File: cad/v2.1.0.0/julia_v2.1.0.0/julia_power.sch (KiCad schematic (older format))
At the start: 50 parts, among them J1 Barrel_Jack_Switch, U2 AZ1117-3.3, U3 AZ1117-2.5, U4 NCP565ST12T3G

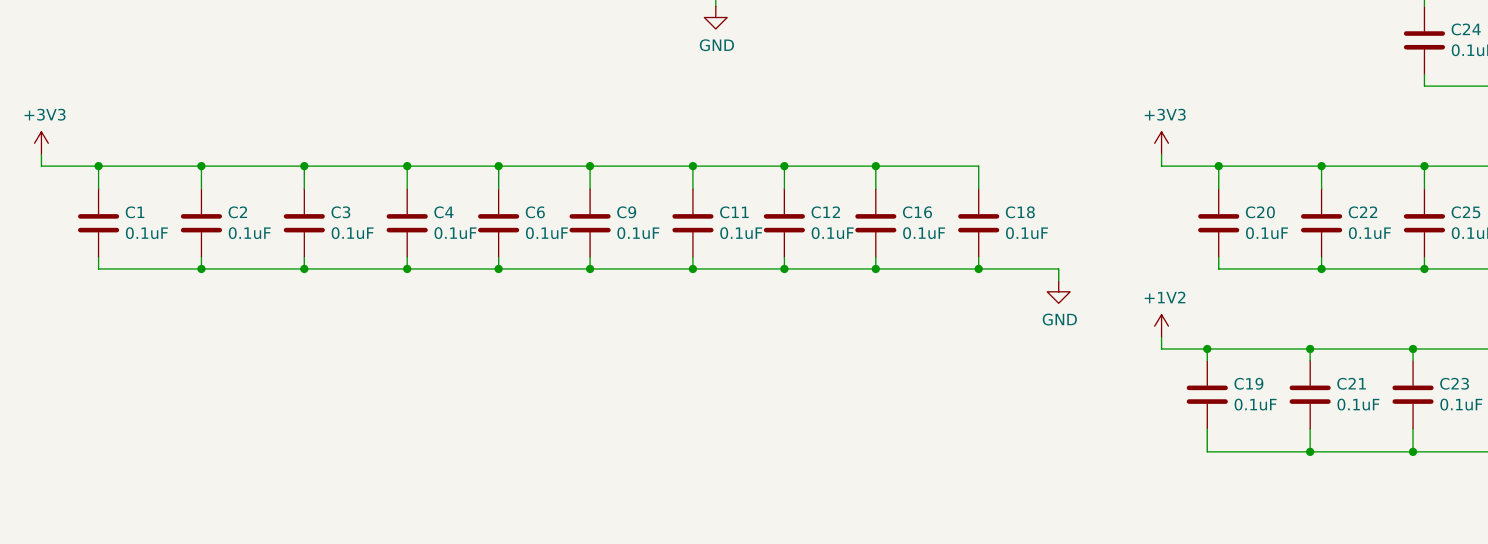
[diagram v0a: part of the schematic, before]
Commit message: v2.1.0.0: changed connector, ERC, annotation/footprint assignment
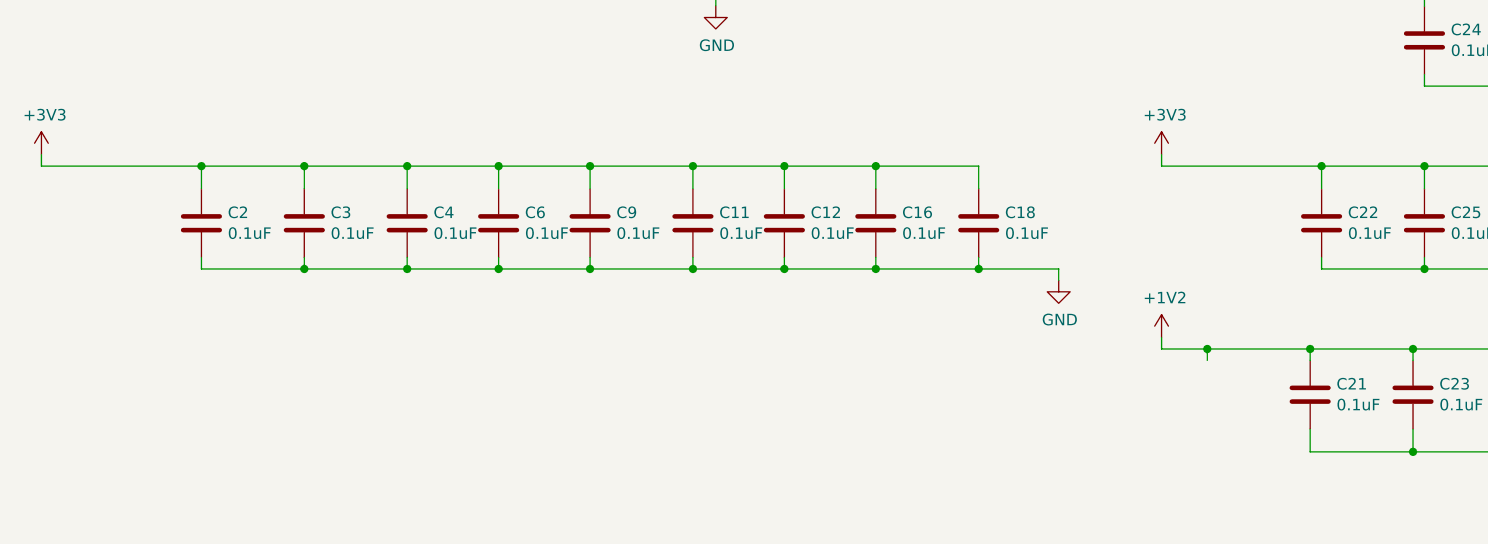
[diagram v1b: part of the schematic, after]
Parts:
- removed C1, C19, C20: 0.1uF, symbol Device:C
- C10, C11, C12, C13, C16, C18, C2, C21, C22, C23, C24, C25, C26, C27, C28, C29, C3, C30, C31, C32, C33, C34, C35, C36, C37, C38, C39, C4, C40, C6, C9: footprint (none) -> Capacitor_SMD:C_0402_1005Metric
- C14, C15, C7, C8: footprint (none) -> Capacitor_SMD:C_0603_1608Metric
- C17, C5: footprint (none) -> Capacitor_Tantalum_SMD:CP_EIA-2012-15_AVX-P
- F1: footprint (none) -> Fuse:Fuse_1206_3216Metric
- J1: footprint (none) -> ik:BarrelJack_GCT_DCJ200-05-A-K1-A_SMD_Horizontal
- TP1, TP2, TP3, TP4, TP5: footprint (none) -> TestPoint:TestPoint_THTPad_D1.0mm_Drill0.5mm
- U2, U3, U4: footprint (none) -> Package_TO_SOT_SMD:SOT-223-3_TabPin2

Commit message: Layout complete(?)
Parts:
- removed C21, C23, C26, C30, C34, C36, C40: 0.1uF, Capacitor_SMD:C_0402_1005Metric, symbol Device:C
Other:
- moved on the sheet: C32, C38
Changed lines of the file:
@@
 $EndComp
 Wire Wire Line
-	9850 6000 9400 6000
-Connection ~ 9850 6000
-Wire Wire Line
-	9850 5900 9850 6000
-Wire Wire Line
-	9400 6000 8950 6000
-Connection ~ 9400 6000
-Wire Wire Line
-	9400 5900 9400 6000
-Wire Wire Line
-	8950 6000 8500 6000
-Connection ~ 8950 6000
-Wire Wire Line
-	8950 5900 8950 6000
-Wire Wire Line
-	8500 6000 8050 6000
-Connection ~ 8500 6000
-Wire Wire Line
-	8500 5900 8500 6000
-Wire Wire Line
-	8050 6000 7600 6000
-Connection ~ 8050 6000
-Wire Wire Line
-	8050 5900 8050 6000
-Wire Wire Line
-	7600 6000 7150 6000
-Connection ~ 7600 6000
-Wire Wire Line
-	7600 5900 7600 6000
-Wire Wire Line
-	7150 6000 6700 6000
-Connection ~ 7150 6000
-Wire Wire Line
-	7150 5900 7150 6000
-Wire Wire Line
-	6700 6000 6250 6000
-Connection ~ 6700 6000
-Wire Wire Line
-	6700 5900 6700 6000
-Wire Wire Line
-	6250 5900 6250 6000
-Wire Wire Line
-	8500 5550 8950 5550
-Connection ~ 8500 5550
-Wire Wire Line
-	8500 5600 8500 5550
-Wire Wire Line
-	8950 5550 9400 5550
-Connection ~ 8950 5550
-Wire Wire Line
-	8950 5600 8950 5550
-Wire Wire Line
-	9400 5550 9850 5550
-Connection ~ 9400 5550
-Wire Wire Line
-	9400 5600 9400 5550
-Wire Wire Line
-	8050 5550 8500 5550
-Connection ~ 8050 5550
-Wire Wire Line
-	8050 5600 8050 5550
-Wire Wire Line
-	7600 5550 8050 5550
-Connection ~ 7600 5550
-Wire Wire Line
-	7600 5600 7600 5550
-Wire Wire Line
-	7150 5550 7600 5550
-Connection ~ 7150 5550
-Wire Wire Line
-	7150 5600 7150 5550
-Wire Wire Line
-	6700 5550 7150 5550
-Connection ~ 6700 5550
-Wire Wire Line
-	6700 5600 6700 5550
-Wire Wire Line
-	6250 5550 6700 5550
-Connection ~ 6250 5550
-Wire Wire Line
-	6250 5600 6250 5550
-Wire Wire Line
-	5800 5550 6250 5550
-Connection ~ 5800 5550
-Wire Wire Line
-	5800 5600 5800 5550
-Wire Wire Line
-	10050 6000 9850 6000
-Wire Wire Line
-	10050 6100 10050 6000
-Wire Wire Line
-	9850 5550 9850 5600
-Wire Wire Line
-	5600 5550 5800 5550
+	6200 5900 6200 6000
+Wire Wire Line
+	5750 5900 5750 6000
+Wire Wire Line
+	6200 5600 6200 5550
+Wire Wire Line
+	5750 5600 5750 5550
+Wire Wire Line
+	6850 6100 6850 6000
 Wire Wire Line
 	5600 5500 5600 5550
@@
 L power:GND #PWR0117
 U 1 1 6020D2AD
-P 10050 6100
-F 0 "#PWR0117" H 10050 5850 50  0001 C CNN
-F 1 "GND" H 10055 5927 50  0000 C CNN
-F 2 "" H 10050 6100 50  0001 C CNN
-F 3 "" H 10050 6100 50  0001 C CNN
-	1    10050 6100
-	1    0    0    -1
-$EndComp
-$Comp
-L Device:C C40
-U 1 1 6020CCFB
-P 9850 5750
-F 0 "C40" H 9965 5796 50  0000 L CNN
-F 1 "0.1uF" H 9965 5705 50  0000 L CNN
-F 2 "Capacitor_SMD:C_0402_1005Metric" H 9888 5600 50  0001 C CNN
-F 3 "~" H 9850 5750 50  0001 C CNN
-	1    9850 5750
+P 6850 6100
+F 0 "#PWR0117" H 6850 5850 50  0001 C CNN
+F 1 "GND" H 6855 5927 50  0000 C CNN
+F 2 "" H 6850 6100 50  0001 C CNN
+F 3 "" H 6850 6100 50  0001 C CNN
+	1    6850 6100
 	1    0    0    -1
 $EndComp
@@
 L Device:C C38
 U 1 1 6020C7C1
-P 9400 5750
-F 0 "C38" H 9515 5796 50  0000 L CNN
-F 1 "0.1uF" H 9515 5705 50  0000 L CNN
-F 2 "Capacitor_SMD:C_0402_1005Metric" H 9438 5600 50  0001 C CNN
-F 3 "~" H 9400 5750 50  0001 C CNN
-	1    9400 5750
-	1    0    0    -1
-$EndComp
-$Comp
-L Device:C C36
-U 1 1 6020C1D4
-P 8950 5750
-F 0 "C36" H 9065 5796 50  0000 L CNN
-F 1 "0.1uF" H 9065 5705 50  0000 L CNN
-F 2 "Capacitor_SMD:C_0402_1005Metric" H 8988 5600 50  0001 C CNN
-F 3 "~" H 8950 5750 50  0001 C CNN
-	1    8950 5750
-	1    0    0    -1
-$EndComp
-$Comp
-L Device:C C34
-U 1 1 6020BC15
-P 8500 5750
-F 0 "C34" H 8615 5796 50  0000 L CNN
-F 1 "0.1uF" H 8615 5705 50  0000 L CNN
-F 2 "Capacitor_SMD:C_0402_1005Metric" H 8538 5600 50  0001 C CNN
-F 3 "~" H 8500 5750 50  0001 C CNN
-	1    8500 5750
+P 6200 5750
+F 0 "C38" H 6315 5796 50  0000 L CNN
+F 1 "0.1uF" H 6315 5705 50  0000 L CNN
+F 2 "Capacitor_SMD:C_0402_1005Metric" H 6238 5600 50  0001 C CNN
+F 3 "~" H 6200 5750 50  0001 C CNN
+	1    6200 5750
 	1    0    0    -1
 $EndComp
@@
 L Device:C C32
 U 1 1 6020B6A5
-P 8050 5750
-F 0 "C32" H 8165 5796 50  0000 L CNN
-F 1 "0.1uF" H 8165 5705 50  0000 L CNN
-F 2 "Capacitor_SMD:C_0402_1005Metric" H 8088 5600 50  0001 C CNN
-F 3 "~" H 8050 5750 50  0001 C CNN
-	1    8050 5750
-	1    0    0    -1
-$EndComp
-$Comp
-L Device:C C30
-U 1 1 6020B1E8
-P 7600 5750
-F 0 "C30" H 7715 5796 50  0000 L CNN
-F 1 "0.1uF" H 7715 5705 50  0000 L CNN
-F 2 "Capacitor_SMD:C_0402_1005Metric" H 7638 5600 50  0001 C CNN
-F 3 "~" H 7600 5750 50  0001 C CNN
-	1    7600 5750
-	1    0    0    -1
-$EndComp
-$Comp
-L Device:C C26
-U 1 1 6020ACC7
-P 7150 5750
-F 0 "C26" H 7265 5796 50  0000 L CNN
-F 1 "0.1uF" H 7265 5705 50  0000 L CNN
-F 2 "Capacitor_SMD:C_0402_1005Metric" H 7188 5600 50  0001 C CNN
-F 3 "~" H 7150 5750 50  0001 C CNN
-	1    7150 5750
-	1    0    0    -1
-$EndComp
-$Comp
-L Device:C C23
-U 1 1 6020A7B8
-P 6700 5750
-F 0 "C23" H 6815 5796 50  0000 L CNN
-F 1 "0.1uF" H 6815 5705 50  0000 L CNN
-F 2 "Capacitor_SMD:C_0402_1005Metric" H 6738 5600 50  0001 C CNN
-F 3 "~" H 6700 5750 50  0001 C CNN
-	1    6700 5750
-	1    0    0    -1
-$EndComp
-$Comp
-L Device:C C21
-U 1 1 6020A22E
-P 6250 5750
-F 0 "C21" H 6365 5796 50  0000 L CNN
-F 1 "0.1uF" H 6365 5705 50  0000 L CNN
-F 2 "Capacitor_SMD:C_0402_1005Metric" H 6288 5600 50  0001 C CNN
-F 3 "~" H 6250 5750 50  0001 C CNN
-	1    6250 5750
+P 5750 5750
+F 0 "C32" H 5865 5796 50  0000 L CNN
+F 1 "0.1uF" H 5865 5705 50  0000 L CNN
+F 2 "Capacitor_SMD:C_0402_1005Metric" H 5788 5600 50  0001 C CNN
+F 3 "~" H 5750 5750 50  0001 C CNN
+	1    5750 5750
 	1    0    0    -1
 $EndComp
@@
 Wire Wire Line
 	5600 4750 6300 4750
+Wire Wire Line
+	6200 6000 6850 6000
+Wire Wire Line
+	5600 5550 5750 5550
+Wire Wire Line
+	6200 5550 5750 5550
+Connection ~ 5750 5550
+Wire Wire Line
+	5750 6000 6200 6000
+Connection ~ 6200 6000
 $EndSCHEMATC
